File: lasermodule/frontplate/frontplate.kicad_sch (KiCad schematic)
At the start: 2 parts

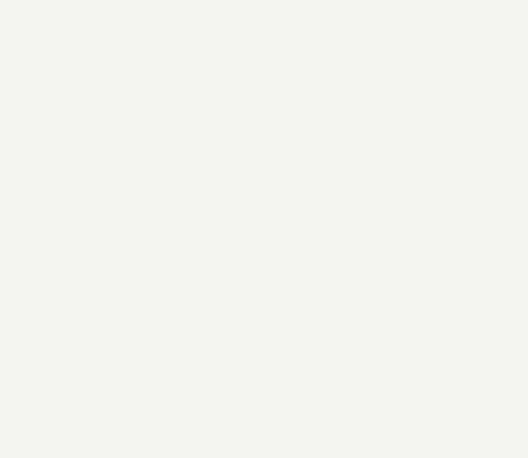
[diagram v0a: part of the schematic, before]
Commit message: removed need for screws using pcb pads
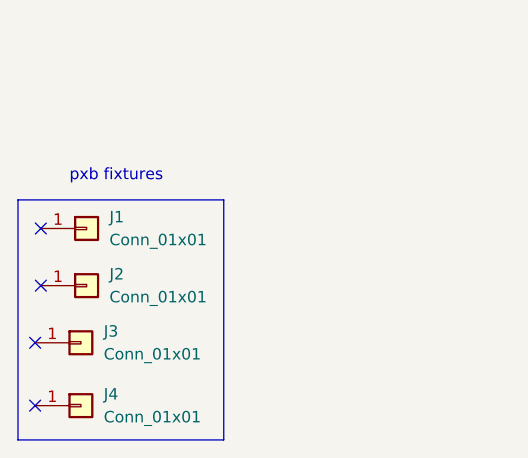
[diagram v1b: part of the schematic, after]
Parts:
- added J1, J2, J3, J4: Conn_01x01, footprints:TestPoint_Pad_2.0x2.0mm_nosilk, symbol Connector_Generic:Conn_01x01
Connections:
- no-connect marks 0 -> 4
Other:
- note added: "pxb fixtures"
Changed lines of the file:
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@@
 (kicad_sch (version 20230121) (generator eeschema)
   (paper "A4")
+  (no_connect (at 59.69 104.14))
+  (no_connect (at 59.69 110.49))
+  (no_connect (at 59.055 116.84))
+  (no_connect (at 59.055 123.825))
+  (polyline (pts (xy 57.15 127.635) (xy 80.01 127.635))
+    (stroke (width 0) (type default))
+  )
+  (polyline (pts (xy 57.15 100.965) (xy 80.01 100.965))
+    (stroke (width 0) (type default))
+  )
+  (polyline (pts (xy 80.01 127.635) (xy 80.01 100.965))
+    (stroke (width 0) (type default))
+  )
+  (polyline (pts (xy 57.15 100.965) (xy 57.15 127.635))
+    (stroke (width 0) (type default))
+  )
+  (text "pxb fixtures" (at 62.865 99.06 0)
+    (effects (font (size 1.27 1.27)) (justify left bottom))
+  )
   (text "hexastorm front" (at 138.43 90.17 0)
     (effects (font (size 1.27 1.27)) (justify left bottom))
@@
         )
       )
+    )
+  )
+  (symbol (lib_id "Connector_Generic:Conn_01x01") (at 64.135 123.825 0) (unit 1)
+    (in_bom yes) (on_board yes) (dnp no) (fields_autoplaced)
+    (property "Reference" "J4" (at 66.675 122.555 0)
+      (effects (font (size 1.27 1.27)) (justify left))
+    )
+    (property "Value" "Conn_01x01" (at 66.675 125.095 0)
+      (effects (font (size 1.27 1.27)) (justify left))
+    )
+    (property "Footprint" "footprints:TestPoint_Pad_2.0x2.0mm_nosilk" (at 64.135 123.825 0)
+      (effects (font (size 1.27 1.27)) hide)
+    )
+    (property "Datasheet" "~" (at 64.135 123.825 0)
+      (effects (font (size 1.27 1.27)) hide)
+    )
+    (pin "1")
+    (instances
+      (project "frontplate"
+        (path "/85697c89-1348-441e-add9-eb5a39865876"
+          (reference "J4") (unit 1)
+        )
+      )
+    )
+  )
+  (symbol (lib_id "Connector_Generic:Conn_01x01") (at 64.135 116.84 0) (unit 1)
+    (in_bom yes) (on_board yes) (dnp no) (fields_autoplaced)
+    (property "Reference" "J3" (at 66.675 115.57 0)
+      (effects (font (size 1.27 1.27)) (justify left))
+    )
+    (property "Value" "Conn_01x01" (at 66.675 118.11 0)
+      (effects (font (size 1.27 1.27)) (justify left))
+    )
+    (property "Footprint" "footprints:TestPoint_Pad_2.0x2.0mm_nosilk" (at 64.135 116.84 0)
+      (effects (font (size 1.27 1.27)) hide)
+    )
+    (property "Datasheet" "~" (at 64.135 116.84 0)
+      (effects (font (size 1.27 1.27)) hide)
+    )
+    (pin "1")
+    (instances
+      (project "frontplate"
+        (path "/85697c89-1348-441e-add9-eb5a39865876"
+          (reference "J3") (unit 1)
+        )
+      )
+    )
+  )
+  (symbol (lib_id "Connector_Generic:Conn_01x01") (at 64.77 110.49 0) (unit 1)
+    (in_bom yes) (on_board yes) (dnp no) (fields_autoplaced)
+    (property "Reference" "J2" (at 67.31 109.22 0)
+      (effects (font (size 1.27 1.27)) (justify left))
+    )
+    (property "Value" "Conn_01x01" (at 67.31 111.76 0)
+      (effects (font (size 1.27 1.27)) (justify left))
+    )
+    (property "Footprint" "footprints:TestPoint_Pad_2.0x2.0mm_nosilk" (at 64.77 110.49 0)
+      (effects (font (size 1.27 1.27)) hide)
+    )
+    (property "Datasheet" "~" (at 64.77 110.49 0)
+      (effects (font (size 1.27 1.27)) hide)
+    )
+    (pin "1")
+    (instances
+      (project "frontplate"
+        (path "/85697c89-1348-441e-add9-eb5a39865876"
+          (reference "J2") (unit 1)
+        )
+      )
+    )
+  )
+  (symbol (lib_id "Connector_Generic:Conn_01x01") (at 64.77 104.14 0) (unit 1)
+    (in_bom yes) (on_board yes) (dnp no) (fields_autoplaced)
+    (property "Reference" "J1" (at 67.31 102.87 0)
+      (effects (font (size 1.27 1.27)) (justify left))
+    )
+    (property "Value" "Conn_01x01" (at 67.31 105.41 0)
+      (effects (font (size 1.27 1.27)) (justify left))
+    )
+    (property "Footprint" "footprints:TestPoint_Pad_2.0x2.0mm_nosilk" (at 64.77 104.14 0)
+      (effects (font (size 1.27 1.27)) hide)
+    )
+    (property "Datasheet" "~" (at 64.77 104.14 0)
+      (effects (font (size 1.27 1.27)) hide)
+    )
+    (pin "1")
+    (instances
+      (project "frontplate"
+        (path "/85697c89-1348-441e-add9-eb5a39865876"
+          (reference "J1") (unit 1)
+        )
+      )

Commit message: board almost fully synced close for release
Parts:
- removed L1, L2: Logo_Open_Hardware_Large, footprints:hexastorm, symbol Graphic:Logo_Open_Hardware_Large
- added J5: pos1, footprints:mirror_pos1, symbol Connector_Generic:Conn_01x01
- added J6: pos2, footprints:mirror_pos2, symbol Connector_Generic:Conn_01x01
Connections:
- net GND: now reaches J1.1 (Pin_1)
- no-connect marks 4 -> 5
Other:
- note added: "fake ground"
- note added: "mirror mounts"
- note removed: "hexastorm back"
- note removed: "hexastorm front"
- moved on the sheet: J3, J4

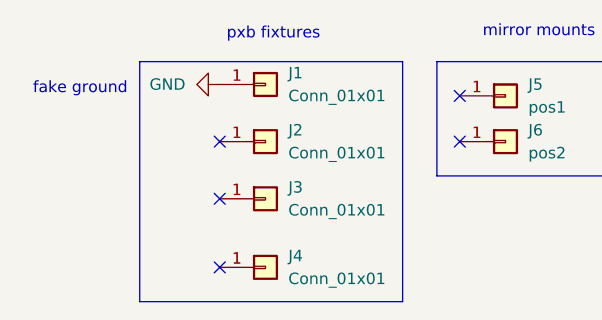
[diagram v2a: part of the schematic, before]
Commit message: added kicost tracking other plates, fixed plates
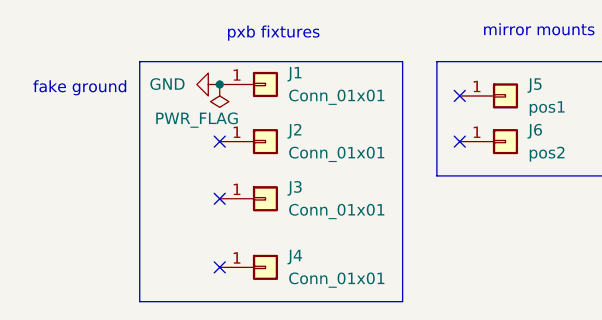
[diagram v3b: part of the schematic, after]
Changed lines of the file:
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@@
 	(generator_version "8.0")
 	(paper "A4")
+	(junction
+		(at 59.69 104.14)
+		(diameter 0)
+		(color 0 0 0 0)
+	)
 	(no_connect
 		(at 59.69 110.49)
@@
 					(unit 1)
 				)
+			)
+		)
+	)
+	(symbol
+		(lib_id "power:PWR_FLAG")
+		(at 59.69 104.14 180)
+		(unit 1)
+		(exclude_from_sim no)
+		(in_bom yes)
+		(on_board yes)
+		(dnp no)
+		(property "Reference" "#FLG01"
+			(at 59.69 106.045 0)
+			(effects
+				(font
+					(size 1.27 1.27)
+				)
+				(hide yes)
+			)
+		)
+		(property "Value" "PWR_FLAG"
+			(at 57.15 107.95 0)
+			(effects
+				(font
+					(size 1.27 1.27)
+				)
+			)
+		)
+		(property "Footprint" ""
+			(at 59.69 104.14 0)
+			(effects
+				(font
+					(size 1.27 1.27)
+				)
+				(hide yes)
+			)
+		)
+		(property "Datasheet" "~"
+			(at 59.69 104.14 0)
+			(effects
+				(font
+					(size 1.27 1.27)
+				)
+				(hide yes)
+			)
+		)
+		(property "Description" "Special symbol for telling ERC where power comes from"
+			(at 59.69 104.14 0)
+			(effects
+				(font
+					(size 1.27 1.27)
+				)
+				(hide yes)
+			)
+		)
+		(pin "1"
+		)
+		(instances
+			(project ""
+				(path "/85697c89-1348-441e-add9-eb5a39865876"
+					(reference "#FLG01")
+					(unit 1)
+				)
